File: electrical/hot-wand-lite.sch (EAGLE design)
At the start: 73 parts, among them IC1 12V R-78K12-2.0, IC2 AMS1117-5.0, Q1 NCHAN, Q2 SIRS5800DP-T1-GE3, Q3 DMTH64M2LPDWQ-13, Q4 2N7002K, U1 SEEED-XIAO-SAMD21, U2 1EDN8511BXUSA1, U3 LM74700QDBVTQ1, U4 AP53781

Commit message: names and part numbers
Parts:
- removed C13_: 470u, hot-wand:CAP_POLPTH4
- removed R17_: 1K, hot-wand:RESISTOR0603-RES
- added C23: 100n, hot-wand:CAP0603-CAP
- added R15: 51K, hot-wand:RESISTOR0603-RES
- added R7: 4K7, hot-wand:RESISTOR0603-RES
- C13: value 10u -> 470u; device hot-wand:CAP_POL1206-KIT -> hot-wand:CAP_POLPTH4; JLC-DNP (none) -> 1; JLCPARTNUM C13585 -> (none); PARTNUM MLASU31LBB5106KTNA01;GRT31CR61H106KE01K -> (none)
- C14: PARTNUM TAJA106K016TNJ;T491A106K016AT -> MLASU31LBB5106KTNA01;GRT31CR61H106KE01K
- C15: device hot-wand:CAP_POL1206 -> hot-wand:CAP_POL1206-KIT
- C16: device hot-wand:CAP_POL1206-KIT -> hot-wand:CAP_POL1206; PARTNUM MLASU31LBB5106KTNA01;GRT31CR61H106KE01K -> TAJA106K016TNJ;T491A106K016AT
- C17: value 100n -> 10u; device hot-wand:CAP0603-CAP -> hot-wand:CAP_POL1206-KIT; JLCPARTNUM C14663 -> C13585; PARTNUM (none) -> MLASU31LBB5106KTNA01;GRT31CR61H106KE01K
- C18: value 1uF -> 100n; JLCPARTNUM C15849 -> C14663
- C19: value 100n -> 1uF; JLCPARTNUM C14663 -> C15849
- R10: value 4K7 -> 100Ω; JLCPARTNUM C23162 -> C22775
- R11: value 4K3 -> 100Ω; JLCPARTNUM C17667 -> C22775
- R12: value 100Ω -> 4K7; JLCPARTNUM C22775 -> C23162
- R13: value 100Ω -> 24K; JLCPARTNUM C22775 -> C23352
- R14: value 4K7 -> 2K; JLCPARTNUM C23162 -> C22975
- R16: value 51K -> 1K; JLCPARTNUM ? -> C21190
- R17: JLCPARTNUM C4211 -> C25803
- R8: value 26K -> 4K7; JLCPARTNUM ? -> C23162
- R9: value 4K7 -> 4K3; JLCPARTNUM C23162 -> C17667
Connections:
- new net N$10: R13.2, R14.1
- net +12V: now also C15.+, C17.+, C19.2; no longer C14.+, C16.+, C17.2
- net +24V: now also C14.+; no longer C13_.+
- net 5V: now also C16.+; no longer C15.+
- net ADC: now also C23.2; no longer C22.2
- net DC-SRC: now also R11.1; no longer R13.1
- net GND: now also C17.-, C20.1, C23.1, R14.2, R16.2, R7.1; no longer C13_.-, C17.1, C21.1, R17_.2, R8.2, R9.1
- net N$30: now also R7.2, R8.2; no longer R10.2, R9.2
- net N$31: now also C20.2, C21.1, R12.1; no longer C19.2, C20.1, R14.1
- net N$32: now also C21.2; no longer C20.2
- net N$36: now also R9.2; no longer R11.2
- net N$37: now also R9.1; no longer R11.1
- net N$38: now also C22.2; no longer C21.2
- net N$39: now also R8.1; no longer R10.1
- net N$40: now also R10.2; no longer R12.2
- net N$42: now also R15.1; no longer R16.1
- net N$43: now also R12.2; no longer R14.2
- net N$57: now also R10.1, R11.2; no longer R12.1, R13.2
- net N$9: now also R15.2, R16.1; no longer R16.2, R17_.1
- net USB-I-SEL: now also R13.1; no longer R8.1
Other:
- note added: "3A default"
- note added: "5A selected"
- moved on the sheet: C13, C14, C15, C16, C18, C19, C20, C21, C22, R10, R11, R12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

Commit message: lite, meas resistors
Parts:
- added SJ1, SJ2, SJ3, SJ4, SJ5: SJ-SMALL-1206-SJ, hot-wand:SJ-SMALL-1206-SJ
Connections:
- new net N$11: Q1.S, SJ1.2
- new net N$12: JP1.2, SJ2.1, SJ3.1, SJ4.1, SJ5.1
- net GND: now also SJ1.1, SJ2.2, SJ3.2, SJ4.2, SJ5.2; no longer JP1.2, Q1.S
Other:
- note added: "4x 0R1 for measurement"
- moved on the sheet: Q1
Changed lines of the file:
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@@
 <attribute name="JLCPARTNUM" value="C22975"/>
 </part>
+<part name="SJ1" library="hot-wand" deviceset="SJ-SMALL" device="-1206-SJ"/>
+<part name="SJ2" library="hot-wand" deviceset="SJ-SMALL" device="-1206-SJ"/>
+<part name="SJ3" library="hot-wand" deviceset="SJ-SMALL" device="-1206-SJ"/>
+<part name="SJ4" library="hot-wand" deviceset="SJ-SMALL" device="-1206-SJ"/>
+<part name="SJ5" library="hot-wand" deviceset="SJ-SMALL" device="-1206-SJ"/>
 </parts>
 <sheets>
@@
 <text x="184.404" y="-556.514" size="1.778" layer="97" align="bottom-right">3A default</text>
 <text x="172.974" y="-569.214" size="1.778" layer="97" rot="R180" align="bottom-right">5A selected</text>
+<text x="180.34" y="-190.5" size="0.6096" layer="97" align="top-left">4x 0R1
+for measurement</text>
 </plain>
 <instances>
@@
 <attribute name="JLCPARTNUM" x="30.48" y="-167.64" size="1.778" layer="96" display="off"/>
 </instance>
-<instance part="JP1" gate="G$1" x="182.88" y="-182.88" rot="MR0">
+<instance part="JP1" gate="G$1" x="182.88" y="-182.88" smashed="yes" rot="MR0">
 <attribute name="PARTNUM" x="182.88" y="-182.88" size="1.778" layer="96" rot="MR0" display="off"/>
 <attribute name="JLC-DNP" x="182.88" y="-182.88" size="1.778" layer="96" rot="MR0" display="off"/>
-</instance>
-<instance part="Q1" gate="G$1" x="30.48" y="-193.04" smashed="yes">
-<attribute name="NAME" x="25.4" y="-187.96" size="1.778" layer="95"/>
-<attribute name="VALUE" x="34.29" y="-187.452" size="1.778" layer="96" rot="R270"/>
-<attribute name="JLC-DNP" x="30.48" y="-193.04" size="1.27" layer="96" display="off"/>
+<attribute name="NAME" x="186.69" y="-178.816" size="1.778" layer="95" rot="MR0"/>
+<attribute name="VALUE" x="186.944" y="-174.498" size="1.778" layer="96" rot="MR0"/>
+</instance>
+<instance part="Q1" gate="G$1" x="30.48" y="-190.5" smashed="yes">
+<attribute name="NAME" x="25.4" y="-185.42" size="1.778" layer="95"/>
+<attribute name="VALUE" x="34.29" y="-184.912" size="1.778" layer="96" rot="R270"/>
+<attribute name="JLC-DNP" x="30.48" y="-190.5" size="1.27" layer="96" display="off"/>
 </instance>
 <instance part="F1" gate="G$1" x="175.26" y="-495.3">
@@
 <attribute name="JLC-DNP" x="144.78" y="-317.5" size="1.778" layer="96" rot="R180" display="off"/>
 </instance>
-<instance part="GND11" gate="1" x="170.18" y="-190.5"/>
+<instance part="GND11" gate="1" x="167.64" y="-198.12"/>
 <instance part="R6" gate="G$1" x="170.18" y="-320.04" smashed="yes" rot="R270">
 <attribute name="NAME" x="170.6626" y="-322.072" size="1.778" layer="95" rot="R270"/>
@@
 <attribute name="JLCPARTNUM" x="185.42" y="-561.34" size="1.778" layer="96" display="off"/>
 </instance>
+<instance part="SJ1" gate="A" x="30.48" y="-198.12" rot="R90"/>
+<instance part="SJ2" gate="A" x="172.72" y="-185.42" rot="R180"/>
+<instance part="SJ3" gate="A" x="172.72" y="-187.96" rot="R180"/>
+<instance part="SJ4" gate="A" x="172.72" y="-190.5" rot="R180"/>
+<instance part="SJ5" gate="A" x="172.72" y="-193.04" rot="R180"/>
 </instances>
 <busses>
@@
 </segment>
 <segment>
-<pinref part="GND2" gate="1" pin="GND"/>
-<pinref part="Q1" gate="G$1" pin="S"/>
-<wire x1="30.48" y1="-200.66" x2="30.48" y2="-198.12" width="0.1524" layer="91"/>
-</segment>
-<segment>
 <pinref part="C1" gate="G$1" pin="2"/>
 <pinref part="GND3" gate="1" pin="GND"/>
@@
 </segment>
 <segment>
-<pinref part="JP1" gate="G$1" pin="2"/>
-<pinref part="GND11" gate="1" pin="GND"/>
-<wire x1="180.34" y1="-182.88" x2="170.18" y2="-182.88" width="0.1524" layer="91"/>
-<wire x1="170.18" y1="-182.88" x2="170.18" y2="-187.96" width="0.1524" layer="91"/>
-</segment>
-<segment>
 <pinref part="JP6" gate="G$1" pin="4"/>
 <pinref part="GND13" gate="1" pin="GND"/>
@@
 <wire x1="190.5" y1="-561.34" x2="193.04" y2="-561.34" width="0.1524" layer="91"/>
 <wire x1="193.04" y1="-561.34" x2="193.04" y2="-563.88" width="0.1524" layer="91"/>
+</segment>
+<segment>
+<pinref part="SJ1" gate="A" pin="1"/>
+<pinref part="GND2" gate="1" pin="GND"/>
+</segment>
+<segment>
+<pinref part="GND11" gate="1" pin="GND"/>
+<pinref part="SJ2" gate="A" pin="2"/>
+<wire x1="167.64" y1="-195.58" x2="167.64" y2="-193.04" width="0.1524" layer="91"/>
+<wire x1="167.64" y1="-193.04" x2="167.64" y2="-190.5" width="0.1524" layer="91"/>
+<wire x1="167.64" y1="-190.5" x2="167.64" y2="-187.96" width="0.1524" layer="91"/>
+<wire x1="167.64" y1="-187.96" x2="167.64" y2="-185.42" width="0.1524" layer="91"/>
+<wire x1="167.64" y1="-185.42" x2="170.18" y2="-185.42" width="0.1524" layer="91"/>
+<pinref part="SJ3" gate="A" pin="2"/>
+<wire x1="170.18" y1="-187.96" x2="167.64" y2="-187.96" width="0.1524" layer="91"/>
+<pinref part="SJ4" gate="A" pin="2"/>
+<wire x1="170.18" y1="-190.5" x2="167.64" y2="-190.5" width="0.1524" layer="91"/>
+<pinref part="SJ5" gate="A" pin="2"/>
+<wire x1="170.18" y1="-193.04" x2="167.64" y2="-193.04" width="0.1524" layer="91"/>
+<junction x="167.64" y="-193.04"/>
+<junction x="167.64" y="-190.5"/>
+<junction x="167.64" y="-187.96"/>
 </segment>
 </net>
@@
 <segment>
 <pinref part="Q1" gate="G$1" pin="G"/>
-<wire x1="22.86" y1="-193.04" x2="20.32" y2="-193.04" width="0.1524" layer="91"/>
-<label x="20.32" y="-193.04" size="1.778" layer="95" rot="R180" xref="yes"/>
+<wire x1="22.86" y1="-190.5" x2="20.32" y2="-190.5" width="0.1524" layer="91"/>
+<label x="20.32" y="-190.5" size="1.778" layer="95" rot="R180" xref="yes"/>
 </segment>
 </net>
@@
 <wire x1="30.48" y1="-175.26" x2="30.48" y2="-180.34" width="0.1524" layer="91"/>
 <pinref part="C2" gate="G$1" pin="1"/>
-<wire x1="30.48" y1="-180.34" x2="30.48" y2="-187.96" width="0.1524" layer="91"/>
+<wire x1="30.48" y1="-180.34" x2="30.48" y2="-185.42" width="0.1524" layer="91"/>
 <wire x1="30.48" y1="-180.34" x2="45.72" y2="-180.34" width="0.1524" layer="91"/>
 <pinref part="C1" gate="G$1" pin="1"/>
@@
 </segment>
 </net>
+<net name="N$11" class="0">
+<segment>
+<pinref part="Q1" gate="G$1" pin="S"/>
+<pinref part="SJ1" gate="A" pin="2"/>
+</segment>
+</net>
+<net name="N$12" class="0">
+<segment>
+<pinref part="JP1" gate="G$1" pin="2"/>
+<wire x1="180.34" y1="-182.88" x2="177.8" y2="-182.88" width="0.1524" layer="91"/>
+<wire x1="177.8" y1="-182.88" x2="177.8" y2="-185.42" width="0.1524" layer="91"/>
+<pinref part="SJ5" gate="A" pin="1"/>
+<wire x1="177.8" y1="-185.42" x2="177.8" y2="-187.96" width="0.1524" layer="91"/>
+<wire x1="177.8" y1="-187.96" x2="177.8" y2="-190.5" width="0.1524" layer="91"/>
+<wire x1="177.8" y1="-190.5" x2="177.8" y2="-193.04" width="0.1524" layer="91"/>
+<wire x1="177.8" y1="-193.04" x2="175.26" y2="-193.04" width="0.1524" layer="91"/>
+<pinref part="SJ4" gate="A" pin="1"/>
+<wire x1="175.26" y1="-190.5" x2="177.8" y2="-190.5" width="0.1524" layer="91"/>
+<pinref part="SJ3" gate="A" pin="1"/>
+<wire x1="175.26" y1="-187.96" x2="177.8" y2="-187.96" width="0.1524" layer="91"/>
+<pinref part="SJ2" gate="A" pin="1"/>
+<wire x1="175.26" y1="-185.42" x2="177.8" y2="-185.42" width="0.1524" layer="91"/>
+<junction x="177.8" y="-185.42"/>
+<junction x="177.8" y="-187.96"/>
+<junction x="177.8" y="-190.5"/>
+</segment>
+</net>

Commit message: lite, moved LED, updated inductor comments
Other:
- note added: "Kool Mu 0077932A7 22 AWG if 2 cores 10 turns if 1 core 14 turns"
- note removed: "Kool Mu 0077932A7 22 AWG if 2 cores 9 or 10 turns if 1 core 18 to 20 turns"
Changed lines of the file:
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@@
 22 AWG
 if 2 cores
-9 or 10 turns
+10 turns
 if 1 core
-18 to 20 turns</text>
+14 turns</text>
 <text x="106.68" y="-182.88" size="0.6096" layer="97" align="top-left">Kool Mu 0077932A7
 22 AWG

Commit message: added selector for 28V
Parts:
- removed JP4: (no value), hot-wand:M06LOCK
- added JP5: (no value), hot-wand:M07LOCK
- added R21: 4K7, hot-wand:RESISTOR0603-RES
- added R22: 470Ω, hot-wand:RESISTOR0603-RES
- R19: value 4K7 -> 51K; JLCPARTNUM C23162 -> C23196
- R20: value 470Ω -> 1K; JLCPARTNUM C23179 -> C21190
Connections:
- removed net USB-V-SEL: JP4.3, R18.2
- new net N$13: R19.2, R20.1
- new net USB-V-SEL-20V: JP5.3, R18.2
- new net USB-V-SEL-28V: JP5.5, R20.2
- net +24V: now also R21.2; no longer R19.2
- net ADC: now also R21.1, R22.1; no longer R19.1, R20.1
- net FAN-CTRL: now also JP5.2; no longer JP4.1
- net GND: now also JP5.1, JP5.4, JP5.7, R22.2; no longer JP4.2, JP4.4, JP4.6, R20.2
- net N$42: now also R19.1
- net USB-I-SEL: now also JP5.6; no longer JP4.5
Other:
- note added: "select 28V (26K eqv)"
- moved on the sheet: R17, R18, R19, R20

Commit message: changing lite pcb to match mosfet changes to other design
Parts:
- added Q5: SIS862ADN-T1-GE3, hot-wand:MOSFET-NCHANNEL-POWERPAK1212-8
- Q2: value SIRS5800DP-T1-GE3 -> SIS862ADN-T1-GE3; device hot-wand:MOSFET-NCHAN-POWERPAKSO8-PPSO8 -> hot-wand:MOSFET-NCHANNEL-POWERPAK1212-8
- R1, R10, R11: device hot-wand:RESISTOR0603-RES -> hot-wand:RESISTOR0805-RES; JLCPARTNUM C22775 -> C441975
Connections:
- new net N$16: Q3A.S, Q5.S, R11.1
- net DC-SRC: now also Q5.D; no longer Q3A.S, R11.1
- net N$37: now also Q5.G
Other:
- note removed: "rated 80V max"
- moved on the sheet: C12, C13, F1, R10, R11, R9

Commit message: update lite design for locking mcu footprint
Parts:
- U1: value SEEED-XIAO-SAMD21 -> SEEED-XIAO-SAMD21-TH-LOCKING; device hot-wand:SEEED-XIAO-SAMD21 -> hot-wand:SEEED-XIAO-SAMD21-TH-LOCKING
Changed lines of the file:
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@@
 <part name="U$1" library="hot-wand" deviceset="5V" device=""/>
 <part name="P+1" library="hot-wand" deviceset="+12V" device=""/>
-<part name="U1" library="hot-wand" deviceset="SEEED-XIAO-SAMD21" device="">
+<part name="U1" library="hot-wand" deviceset="SEEED-XIAO-SAMD21" device="-TH-LOCKING" value="SEEED-XIAO-SAMD21-TH-LOCKING">
 <attribute name="JLC-DNP" value="1"/>
 </part>

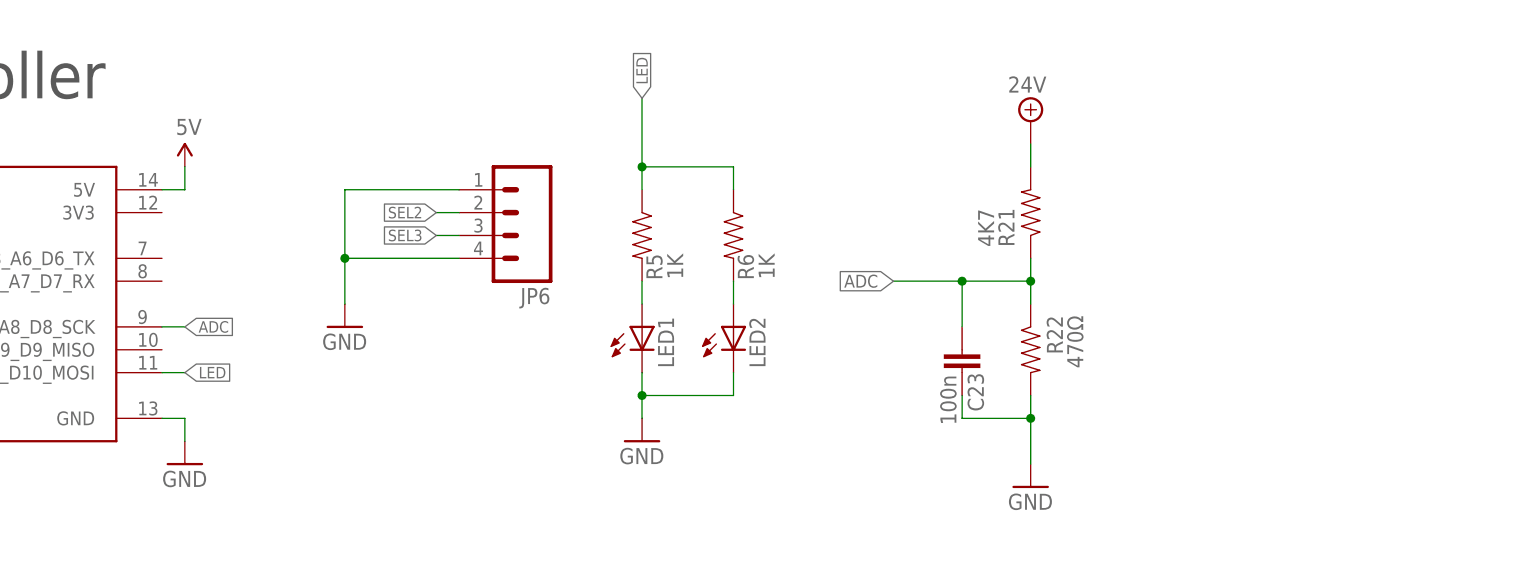
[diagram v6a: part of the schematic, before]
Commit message: added power disable signal to lite MCU
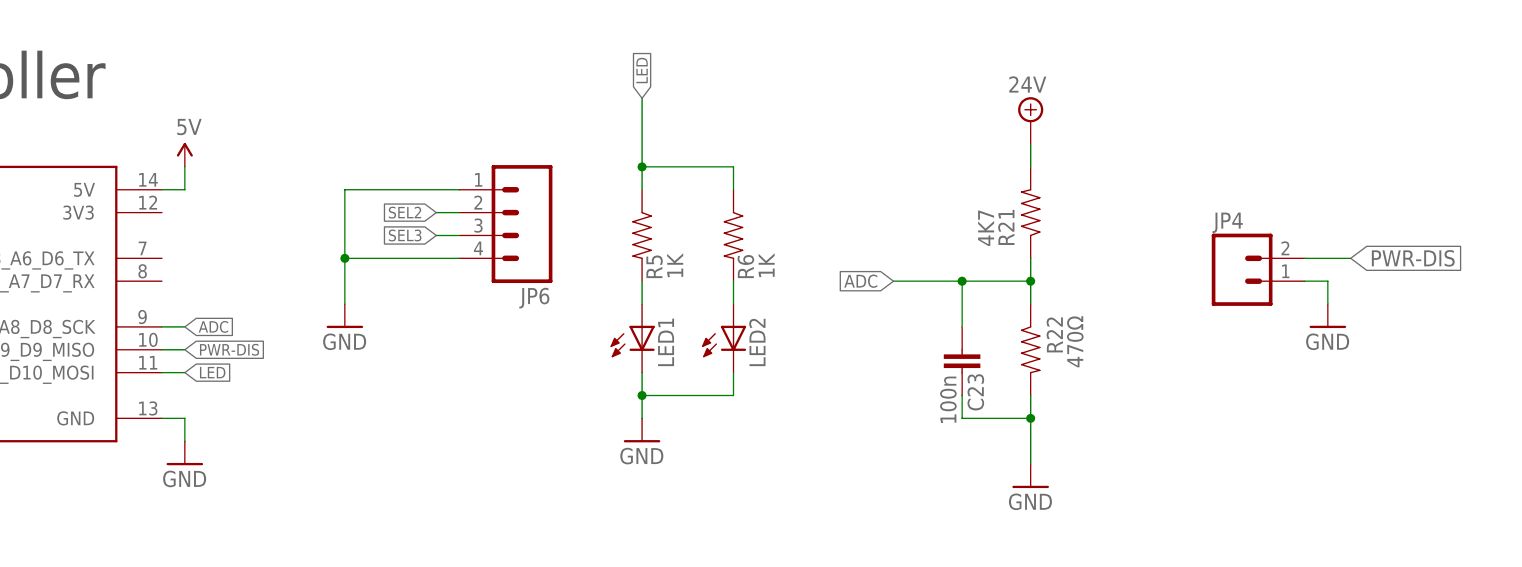
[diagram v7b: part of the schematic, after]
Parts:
- added JP4: (no value), hot-wand:M02PTH3
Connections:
- new net PWR-DIS: JP4.2, U1.PA5_A9_D9_MISO
- net GND: now also JP4.1
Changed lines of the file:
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@@
 <attribute name="JLC-DNP" value="1"/>
 </part>
+<part name="JP4" library="hot-wand" deviceset="M02" device="PTH3"/>
+<part name="GND10" library="hot-wand" deviceset="GND" device=""/>
 </parts>
 <sheets>
@@
 <attribute name="VALUE" x="187.706" y="-521.97" size="1.778" layer="96" rot="MR0"/>
 </instance>
+<instance part="JP4" gate="G$1" x="226.06" y="-325.12"/>
+<instance part="GND10" gate="1" x="236.22" y="-330.2"/>
 </instances>
 <busses>
@@
 <wire x1="228.6" y1="-589.28" x2="226.06" y2="-589.28" width="0.1524" layer="91"/>
 <label x="226.06" y="-589.28" size="1.27" layer="95" rot="R180" xref="yes"/>
+</segment>
+<segment>
+<pinref part="JP4" gate="G$1" pin="1"/>
+<pinref part="GND10" gate="1" pin="GND"/>
+<wire x1="233.68" y1="-325.12" x2="236.22" y2="-325.12" width="0.1524" layer="91"/>
+<wire x1="236.22" y1="-325.12" x2="236.22" y2="-327.66" width="0.1524" layer="91"/>
 </segment>
 </net>
@@
 </segment>
 </net>
+<net name="PWR-DIS" class="0">
+<segment>
+<pinref part="U1" gate="G$1" pin="PA5_A9_D9_MISO"/>
+<wire x1="106.68" y1="-332.74" x2="109.22" y2="-332.74" width="0.1524" layer="91"/>
+<label x="109.22" y="-332.74" size="1.27" layer="95" xref="yes"/>
+</segment>
+<segment>
+<pinref part="JP4" gate="G$1" pin="2"/>
+<wire x1="233.68" y1="-322.58" x2="238.76" y2="-322.58" width="0.1524" layer="91"/>
+<label x="238.76" y="-322.58" size="1.778" layer="95" xref="yes"/>
+</segment>
+</net>
